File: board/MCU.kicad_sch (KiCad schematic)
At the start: 3 parts

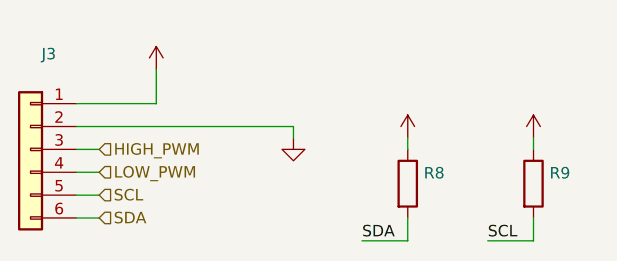
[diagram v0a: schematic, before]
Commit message: Different board layout, WIP
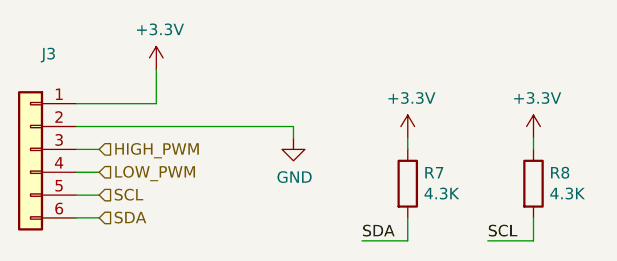
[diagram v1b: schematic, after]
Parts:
- J3: value (none) -> Conn_01x06; footprint (none) -> Connector_PinHeader_2.54mm:PinHeader_1x06_P2.54mm_Vertical
- R7: renamed from R8; value (none) -> 4.3K; footprint (none) -> Resistor_SMD:R_0805_2012Metric_Pad1.20x1.40mm_HandSolder
- R8: renamed from R9; value (none) -> 4.3K; footprint (none) -> Resistor_SMD:R_0805_2012Metric_Pad1.20x1.40mm_HandSolder
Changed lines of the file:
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@@
     (in_bom yes) (on_board yes)
     (property "Reference" "J3" (id 0) (at 73.152 59.2582 0))
-    (property "Value" "" (id 1) (at 73.152 61.5696 0)
+    (property "Value" "Conn_01x06" (id 1) (at 73.152 61.5696 0)
       (effects (font (size 1.27 1.27)) hide)
     )
-    (property "Footprint" "" (id 2) (at 71.12 69.85 0)
+    (property "Footprint" "Connector_PinHeader_2.54mm:PinHeader_1x06_P2.54mm_Vertical" (id 2) (at 71.12 69.85 0)
       (effects (font (size 1.27 1.27)) hide)
     )
@@
   (symbol (lib_id "power:+3.3V") (at 85.09 60.96 0) (unit 1)
     (in_bom yes) (on_board yes)
-    (property "Reference" "#PWR020" (id 0) (at 85.09 64.77 0)
+    (property "Reference" "#PWR019" (id 0) (at 85.09 64.77 0)
       (effects (font (size 1.27 1.27)) hide)
     )
-    (property "Value" "" (id 1) (at 85.471 56.5658 0))
+    (property "Value" "+3.3V" (id 1) (at 85.471 56.5658 0))
     (property "Footprint" "" (id 2) (at 85.09 60.96 0)
       (effects (font (size 1.27 1.27)) hide)
@@
   (symbol (lib_id "power:GND") (at 100.33 68.58 0) (unit 1)
     (in_bom yes) (on_board yes)
-    (property "Reference" "#PWR021" (id 0) (at 100.33 74.93 0)
+    (property "Reference" "#PWR020" (id 0) (at 100.33 74.93 0)
       (effects (font (size 1.27 1.27)) hide)
     )
-    (property "Value" "" (id 1) (at 100.457 72.9742 0))
+    (property "Value" "GND" (id 1) (at 100.457 72.9742 0))
     (property "Footprint" "" (id 2) (at 100.33 68.58 0)
       (effects (font (size 1.27 1.27)) hide)
@@
   (symbol (lib_id "power:+3.3V") (at 113.03 68.58 0) (unit 1)
     (in_bom yes) (on_board yes)
-    (property "Reference" "#PWR022" (id 0) (at 113.03 72.39 0)
+    (property "Reference" "#PWR021" (id 0) (at 113.03 72.39 0)
       (effects (font (size 1.27 1.27)) hide)
     )
-    (property "Value" "" (id 1) (at 113.411 64.1858 0))
+    (property "Value" "+3.3V" (id 1) (at 113.411 64.1858 0))
     (property "Footprint" "" (id 2) (at 113.03 68.58 0)
       (effects (font (size 1.27 1.27)) hide)
@@
   (symbol (lib_id "Device:R") (at 113.03 73.66 0) (unit 1)
     (in_bom yes) (on_board yes)
-    (property "Reference" "R8" (id 0) (at 114.808 72.4916 0)
+    (property "Reference" "R7" (id 0) (at 114.808 72.4916 0)
       (effects (font (size 1.27 1.27)) (justify left))
     )
-    (property "Value" "" (id 1) (at 114.808 74.803 0)
+    (property "Value" "4.3K" (id 1) (at 114.808 74.803 0)
       (effects (font (size 1.27 1.27)) (justify left))
     )
-    (property "Footprint" "" (id 2) (at 111.252 73.66 90)
+    (property "Footprint" "Resistor_SMD:R_0805_2012Metric_Pad1.20x1.40mm_HandSolder" (id 2) (at 111.252 73.66 90)
       (effects (font (size 1.27 1.27)) hide)
     )
@@
   (symbol (lib_id "power:+3.3V") (at 127 68.58 0) (unit 1)
     (in_bom yes) (on_board yes)
-    (property "Reference" "#PWR023" (id 0) (at 127 72.39 0)
+    (property "Reference" "#PWR022" (id 0) (at 127 72.39 0)
       (effects (font (size 1.27 1.27)) hide)
     )
-    (property "Value" "" (id 1) (at 127.381 64.1858 0))
+    (property "Value" "+3.3V" (id 1) (at 127.381 64.1858 0))
     (property "Footprint" "" (id 2) (at 127 68.58 0)
       (effects (font (size 1.27 1.27)) hide)
@@
   (symbol (lib_id "Device:R") (at 127 73.66 0) (unit 1)
     (in_bom yes) (on_board yes)
-    (property "Reference" "R9" (id 0) (at 128.778 72.4916 0)
+    (property "Reference" "R8" (id 0) (at 128.778 72.4916 0)
       (effects (font (size 1.27 1.27)) (justify left))
     )
-    (property "Value" "" (id 1) (at 128.778 74.803 0)
+    (property "Value" "4.3K" (id 1) (at 128.778 74.803 0)
       (effects (font (size 1.27 1.27)) (justify left))
     )
-    (property "Footprint" "" (id 2) (at 125.222 73.66 90)
+    (property "Footprint" "Resistor_SMD:R_0805_2012Metric_Pad1.20x1.40mm_HandSolder" (id 2) (at 125.222 73.66 90)
       (effects (font (size 1.27 1.27)) hide)
     )
